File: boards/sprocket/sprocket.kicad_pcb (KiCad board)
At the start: 2 copper layers, 47 x 15 mm, 14 parts, among them U1 STM32G031F8P6

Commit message: I don't know what this branch is
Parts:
- removed the MH at (144.0, 104.0)
- removed the MH at (104.0, 104.0)
- removed the REF** at (125.2, 104.5)
- removed the REF** at (120.0, 103.8)
- removed the REF** at (112.0, 103.8)
- removed the REF** at (129.0, 111.0)
- removed the REF** at (129.0, 112.8)
- removed the REF** at (129.0, 114.5)
- removed the REF** at (132.8, 112.5)
- removed the REF** at (137.5, 112.5)
- removed the REF** at (130.0, 102.8)
- removed the REF** at (109.7, 113.5)
- removed the REF** at (109.7, 111.0)
- removed U1: STM32G031F8P6, footprints:STM32G031F8P6
- added MH: brick-1x2, brick-4_9id-6_0od:brick-1x2, F.Cu at (126.1, 92.0)
- added MH: brick-1x2, brick-4_9id-6_0od:brick-1x2, F.Cu at (166.1, 92.0)
- added REF**: C_0603_1608Metric, Capacitor_SMD:C_0603_1608Metric, F.Cu at (138.5, 101.6)
- added REF**: SW_SPST_PTS810, Button_Switch_SMD:SW_SPST_PTS810, F.Cu at (142.3, 101.0)
- added REF**: SW_SPST_PTS810, Button_Switch_SMD:SW_SPST_PTS810, F.Cu at (142.3, 91.0)
- added REF**: UQFN-28-1EP_4x4mm_P0.4mm_EP2.35x2.35mm, Package_DFN_QFN:UQFN-28-1EP_4x4mm_P0.4mm_EP2.35x2.35mm, F.Cu at (137.3, 96.0)
- added REF**: SOT-23, Package_TO_SOT_SMD:SOT-23, F.Cu at (142.0, 96.0)
- added REF**: JST_SH_BM04B-SRSS-TB_1x04-1MP_P1.00mm_Vertical, Connector_JST:JST_SH_BM04B-SRSS-TB_1x04-1MP_P1.00mm_Vertical, B.Cu at (141.9, 100.8)
- added REF**: JST_SH_BM04B-SRSS-TB_1x04-1MP_P1.00mm_Vertical, Connector_JST:JST_SH_BM04B-SRSS-TB_1x04-1MP_P1.00mm_Vertical, B.Cu at (141.9, 91.2)
- added REF**: JST_SH_SM04B-SRSS-TB_1x04-1MP_P1.00mm_Horizontal, Connector_JST:JST_SH_SM04B-SRSS-TB_1x04-1MP_P1.00mm_Horizontal, B.Cu at (134.1, 100.2)
- added REF**: JST_SH_SM04B-SRSS-TB_1x04-1MP_P1.00mm_Horizontal, Connector_JST:JST_SH_SM04B-SRSS-TB_1x04-1MP_P1.00mm_Horizontal, B.Cu at (134.1, 91.8)
- added REF**: PinHeader_1x06_P2.54mm_Vertical, Connector_PinHeader_2.54mm:PinHeader_1x06_P2.54mm_Vertical, F.Cu at (147.2, 96.0)
- added REF**: PinSocket_2x06_P2.54mm_Horizontal, Connector_PinSocket_2.54mm:PinSocket_2x06_P2.54mm_Horizontal, F.Cu at (147.2, 98.5)
- added REF**: C_0603_1608Metric, Capacitor_SMD:C_0603_1608Metric, F.Cu at (138.5, 90.5)
- added REF**: PinSocket_2x06_P2.54mm_Horizontal, Connector_PinSocket_2.54mm:PinSocket_2x06_P2.54mm_Horizontal, F.Cu at (159.9, 93.5)
- added REF**: R_0603_1608Metric, Resistor_SMD:R_0603_1608Metric, F.Cu at (136.3, 100.8)
- added REF**: R_0603_1608Metric, Resistor_SMD:R_0603_1608Metric, F.Cu at (136.3, 91.2)
- added REF**: C_0603_1608Metric, Capacitor_SMD:C_0603_1608Metric, F.Cu at (144.5, 94.5)
- added REF**: C_0603_1608Metric, Capacitor_SMD:C_0603_1608Metric, F.Cu at (144.5, 97.5)
- added REF**: C_0603_1608Metric, Capacitor_SMD:C_0603_1608Metric, F.Cu at (136.3, 102.3)
- added REF**: C_0603_1608Metric, Capacitor_SMD:C_0603_1608Metric, F.Cu at (136.3, 89.7)
- added REF**: SOT-23, Package_TO_SOT_SMD:SOT-23, F.Cu at (131.9, 96.0)
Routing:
- net (no net): track 0.00 -> 0.25 mm, vias 0 -> 6
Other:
- rule trace_min: 0.2 -> 0.09
- rule via_min_drill: 0.3 -> 0.2
- board text added: "0.0164"
- board text added: "0.0250"
- board text added: "0.0621"
- board text added: "4.2x3.25"
- board text added: "5.1x5.1"
- board text added: "6.0x6.0"
- board text added: "Cheap Round: TS-1187A-C-E-B"
- board text added: "Close, but not EXACTLY footprint as above"
- board text added: "Digital Port"
- board text added: "GND"
- board text added: "GPIO port"
- board text added: "LED"
- board text added: "One Space Horizontal, maybe Vertical"
- board text added: "Oval Switch: K2-1808SN-A4SW-01"
- board text added: "Programming/Debugging Port"
- board text added: "RGB LED"
- board text added: "Round Switch: K2-1102SP-C4SC-04"
- board text added: "SCL"
- board text added: "SDA"
- board text added: "VCC"

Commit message: Work
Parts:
- removed MH (x2): brick-1x2, brick-4_9id-6_0od:brick-1x2
- removed REF** (x6): C_0603_1608Metric, Capacitor_SMD:C_0603_1608Metric
- removed REF** (x2): SW_SPST_PTS810, Button_Switch_SMD:SW_SPST_PTS810
- removed REF**: UQFN-28-1EP_4x4mm_P0.4mm_EP2.35x2.35mm, Package_DFN_QFN:UQFN-28-1EP_4x4mm_P0.4mm_EP2.35x2.35mm
- removed REF** (x2): SOT-23, Package_TO_SOT_SMD:SOT-23
- removed REF** (x2): JST_SH_BM04B-SRSS-TB_1x04-1MP_P1.00mm_Vertical, Connector_JST:JST_SH_BM04B-SRSS-TB_1x04-1MP_P1.00mm_Vertical
- removed REF** (x2): JST_SH_SM04B-SRSS-TB_1x04-1MP_P1.00mm_Horizontal, Connector_JST:JST_SH_SM04B-SRSS-TB_1x04-1MP_P1.00mm_Horizontal
- removed REF**: PinHeader_1x06_P2.54mm_Vertical, Connector_PinHeader_2.54mm:PinHeader_1x06_P2.54mm_Vertical
- removed REF** (x2): PinSocket_2x06_P2.54mm_Horizontal, Connector_PinSocket_2.54mm:PinSocket_2x06_P2.54mm_Horizontal
- removed REF** (x2): R_0603_1608Metric, Resistor_SMD:R_0603_1608Metric
- added C1: 100nF, Capacitor_SMD:C_0402_1005Metric, F.Cu at (117.6, 85.2)
- added C2: 100nF, Capacitor_SMD:C_0402_1005Metric, F.Cu at (117.6, 83.3)
- added C3: 4.7uF, Capacitor_SMD:C_0402_1005Metric, F.Cu at (118.6, 85.2)
- added C4: 1uF, Capacitor_SMD:C_0402_1005Metric, F.Cu at (119.0, 82.6)
- added C5: 2.2uF, Capacitor_SMD:C_0603_1608Metric, F.Cu at (121.5, 85.9)
- added C6: 1uF, Capacitor_SMD:C_0402_1005Metric, F.Cu at (108.6, 87.8)
- added C7: 1uF, Capacitor_SMD:C_0402_1005Metric, F.Cu at (108.6, 77.0)
- added D1: B5819W, Diode_SMD:D_SOD-123, F.Cu at (120.8, 80.4)
- added D2: TC3838RGB, Everything:TC3838RGB, F.Cu at (109.2, 87.0)
- added D3: TC3838RGB, Everything:TC3838RGB, F.Cu at (109.2, 76.2)
- added D4: LED, Diode_SMD:D_0603_1608Metric, F.Cu at (110.5, 84.5)
- added D5: LED, Diode_SMD:D_0603_1608Metric, F.Cu at (109.0, 84.5)
- added D6: LED, Diode_SMD:D_0603_1608Metric, F.Cu at (109.0, 81.2)
- added J1: SPROCKET-CONN, Everything:sprocket-pins, F.Cu at (123.6, 90.6)
- added J4: Conn_01x04_MountingPin, Connector_JST:JST_SH_SM04B-SRSS-TB_1x04-1MP_P1.00mm_Horizontal, B.Cu at (120.7, 87.2)
- added J5: Conn_01x04_MountingPin, Connector_JST:JST_SH_BM04B-SRSS-TB_1x04-1MP_P1.00mm_Vertical, B.Cu at (112.4, 87.9)
- added J6: Conn_01x04_MountingPin, Connector_JST:JST_SH_SM04B-SRSS-TB_1x04-1MP_P1.00mm_Horizontal, B.Cu at (112.4, 78.8)
- added J7: Conn_01x04_MountingPin, Connector_JST:JST_SH_BM04B-SRSS-TB_1x04-1MP_P1.00mm_Vertical, B.Cu at (120.7, 78.1)
- added JP1: SolderJumper_2_Open, Jumper:SolderJumper-2_P1.3mm_Open_TrianglePad1.0x1.5mm, B.Cu at (139.7, 127.0)
- added JP2: SolderJumper_2_Open, Jumper:SolderJumper-2_P1.3mm_Open_TrianglePad1.0x1.5mm, B.Cu at (126.1, 124.7)
- added JP3: SolderJumper_2_Open, Jumper:SolderJumper-2_P1.3mm_Open_TrianglePad1.0x1.5mm, B.Cu at (128.3, 117.6)
- added JP4: SolderJumper_2_Open, Jumper:SolderJumper-2_P1.3mm_Open_TrianglePad1.0x1.5mm, B.Cu at (128.5, 132.0)
- added JP5: SolderJumper_2_Open, Jumper:SolderJumper-2_P1.3mm_Open_TrianglePad1.0x1.5mm, B.Cu at (132.7, 116.3)
- added JP6: SolderJumper_2_Open, Jumper:SolderJumper-2_P1.3mm_Open_TrianglePad1.0x1.5mm, B.Cu at (130.5, 124.7)
- added MH1: Conn_01x02, brick-4_9id-6_0od:brick-1x2, F.Cu at (104.0, 79.0)
- added MH2: Conn_01x02, brick-4_9id-6_0od:brick-1x2, F.Cu at (144.0, 79.0)
- added Q1: NX7002BKR, Package_TO_SOT_SMD:SOT-23, F.Cu at (115.2, 77.5)
- added R1: 10K, Resistor_SMD:R_0402_1005Metric, F.Cu at (116.4, 89.3)
- added R2: 10K, Resistor_SMD:R_0402_1005Metric, F.Cu at (117.5, 76.7)
- added R3: 10K, Resistor_SMD:R_0402_1005Metric, F.Cu at (116.0, 79.8)
- added R4: 1K, Resistor_SMD:R_0402_1005Metric, F.Cu at (117.4, 89.3)
- added R5: 1K, Resistor_SMD:R_0402_1005Metric, F.Cu at (117.5, 78.6)
- added R6: 1K, Resistor_SMD:R_0402_1005Metric, F.Cu at (110.7, 81.5)
- added R7: 1K, Resistor_SMD:R_0402_1005Metric, F.Cu at (110.7, 82.5)
- added R8: 1K, Resistor_SMD:R_0402_1005Metric, F.Cu at (110.7, 80.5)
- added SW1: SW_Push, Everything:K2-1808SN-A4SW-01, F.Cu at (118.2, 87.2)
- added SW2: SW_Push, Everything:K2-1808SN-A4SW-01, F.Cu at (123.8, 78.7)
- added U1: UFQFPN-28, footprints:STM32G031G8U6, F.Cu at (114.4, 84.3)
- added U2: AP2210N-3.3TRG1, Package_TO_SOT_SMD:SOT-23, F.Cu at (121.3, 83.4)
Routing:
- net (no net): track 0.25 -> 0.00 mm, vias 6 -> 0
- added copper zone on B.Cu, net GND
- added copper zone on F.Cu, net GND
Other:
- copper layers 2 -> 4
- rule trace_min: 0.09 -> 0.2
- board text added: "TODO: Move buttons to top, LEDs to bottom"
- board text removed: "0.0164"
- board text removed: "0.0250"
- board text removed: "0.0621"
- board text removed: "4.2x3.25"
- board text removed: "5.1x5.1"
- board text removed: "6.0x6.0"
- board text removed: "Cheap Round: TS-1187A-C-E-B"
- board text removed: "Close, but not EXACTLY footprint as above"
- board text removed: "Digital Port"
- board text removed: "GND"
- board text removed: "GPIO port"
- board text removed: "LED"
- board text removed: "One Space Horizontal, maybe Vertical"
- board text removed: "Oval Switch: K2-1808SN-A4SW-01"
- board text removed: "Programming/Debugging Port"
- board text removed: "RGB LED"
- board text removed: "Round Switch: K2-1102SP-C4SC-04"
- board text removed: "SCL"
- board text removed: "SDA"
- board text removed: "VCC"

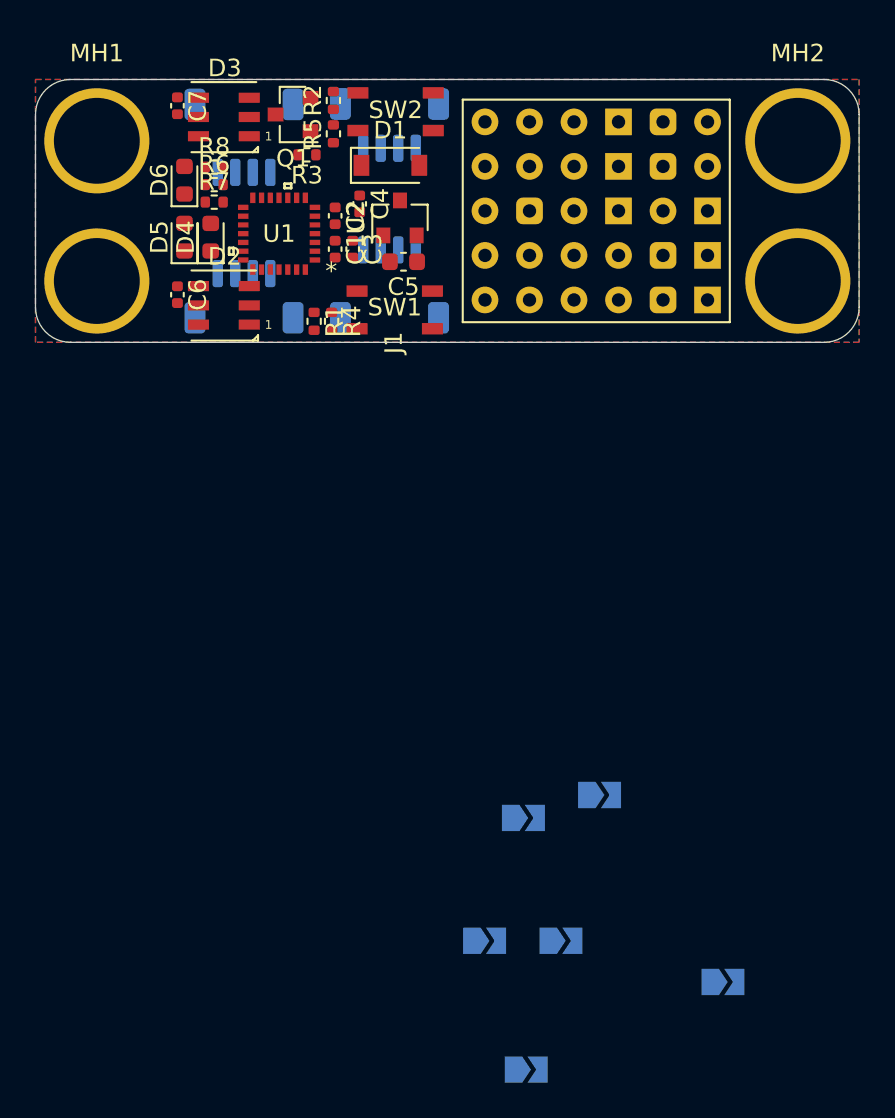
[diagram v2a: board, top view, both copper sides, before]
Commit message: Re-place, pre-route
Trying to keep the 5V low, and the center path clear
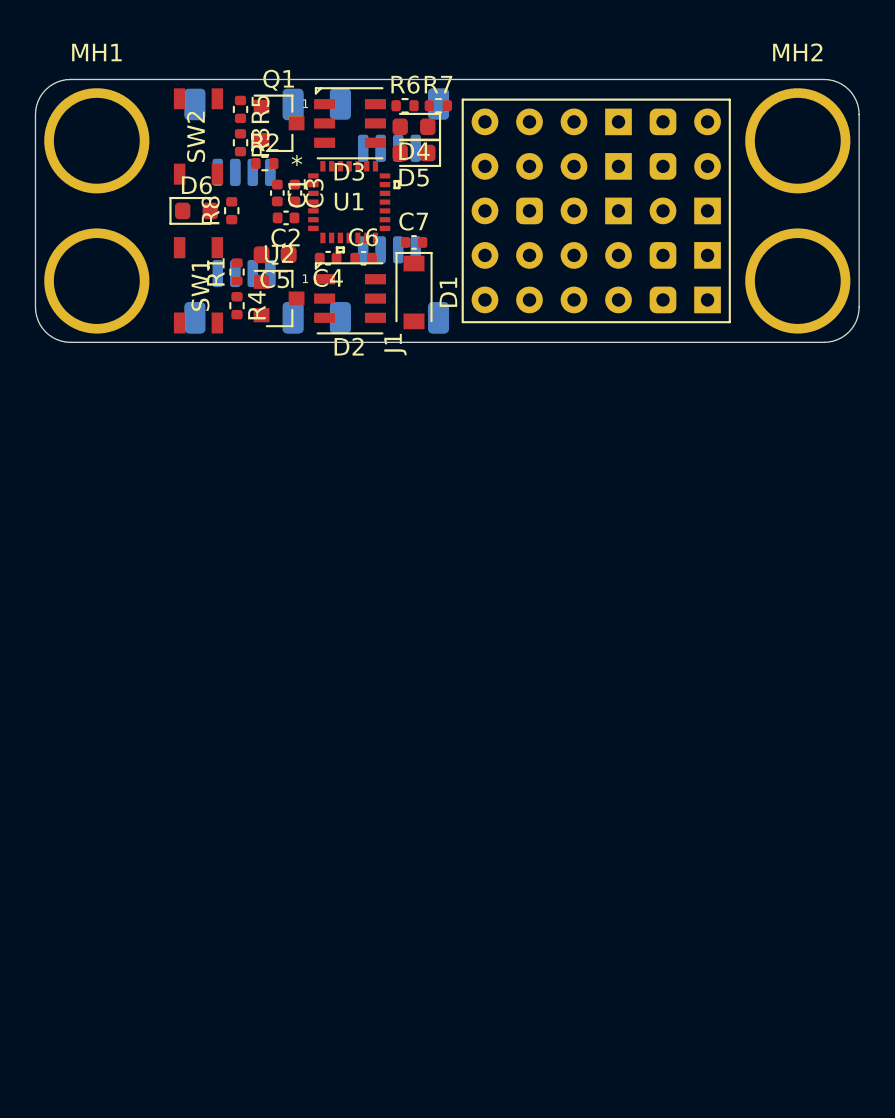
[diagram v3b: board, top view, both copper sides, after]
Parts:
- removed JP1, JP2, JP3, JP4, JP5, JP6: SolderJumper_2_Open, Jumper:SolderJumper-2_P1.3mm_Open_TrianglePad1.0x1.5mm
- U1: value UFQFPN-28 -> STM32G031G8U6
- moved C7 15.6 mm to (122.1, 84.8), turned to 0 degrees
- moved D5 14.0 mm to (122.1, 79.7), turned to 180 degrees
- moved R7 13.9 mm to (123.5, 77.0)
- moved D4 13.2 mm to (122.1, 78.2), turned to 180 degrees
- moved SW2 12.9 mm to (111.2, 76.0), turned to 270 degrees
- moved R6 11.8 mm to (121.6, 77.0)
- moved D3 11.7 mm to (120.5, 79.4), turned to 180 degrees
- moved D2 11.5 mm to (120.5, 89.4), turned to 180 degrees
- moved C6 10.8 mm to (119.2, 85.7), turned to 0 degrees
- moved U2 8.29 mm to (114.4, 88.0), turned to 0 degrees
- moved SW1 7.57 mm to (111.2, 84.5), turned to 270 degrees
- moved D1 7.37 mm to (122.1, 87.7), turned to 270 degrees
- moved C5 7.34 mm to (114.2, 85.5)
- moved R5 5.48 mm to (112.2, 77.2), turned to 270 degrees
- moved R4 5.47 mm to (112.0, 88.4)
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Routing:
- added copper zone on In2.Cu, net +3V3
- added copper zone on In1.Cu, net GND
- removed copper zone on B.Cu, net GND
- removed copper zone on F.Cu, net GND

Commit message: Dead end-ish, going to re-wipe and retry
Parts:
- moved R4 11.2 mm to (112.2, 77.2)
- moved R5 11.2 mm to (112.0, 88.4), turned to 90 degrees
- moved SW1 8.50 mm to (111.2, 76.0)
- moved SW2 8.50 mm to (111.2, 84.5)
- moved R3 2.60 mm to (114.5, 80.3), turned to 180 degrees
- moved R2 1.84 mm to (112.2, 79.1), turned to 270 degrees
- turned R1 to 270 degrees
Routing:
- net GND: track 0.00 -> 53.0 mm, vias 0 -> 9
- net /+5v0-RAW: track 0.00 -> 39.6 mm, vias 0 -> 1
- net +3V3: track 0.00 -> 34.5 mm, vias 0 -> 5
- net /I2C1-SDA: track 0.00 -> 33.9 mm, vias 0 -> 4
- net +5V: track 0.00 -> 31.1 mm
- net /I2C1-SCL: track 0.00 -> 28.4 mm, vias 0 -> 2
- net /~RST: track 0.00 -> 23.6 mm, vias 0 -> 2
- net /GPIO4: track 0.00 -> 17.1 mm, vias 0 -> 2
- net /BUTTON2: track 0.00 -> 16.8 mm, vias 0 -> 2
- net /GPIO3: track 0.00 -> 16.2 mm, vias 0 -> 2
- net /GPIO8: track 0.00 -> 14.4 mm
- net /I2C2-SCL: track 0.00 -> 14.1 mm, vias 0 -> 1
- net /LED1: track 0.00 -> 13.2 mm, vias 0 -> 2
- net /BUTTON1: track 0.00 -> 12.9 mm, vias 0 -> 2
- net /SMARTLED-3V3: track 0.00 -> 12.5 mm, vias 0 -> 2
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- added copper zone on B.Cu, net GND

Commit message: Gunna bail.
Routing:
- net +5V: track 31.1 -> 67.0 mm, vias 0 -> 6
- net /UART-TX: track 0.00 -> 32.6 mm, vias 0 -> 2
- net /UART-RX: track 0.00 -> 28.0 mm, vias 0 -> 2
- net +3V3: track 34.5 -> 61.2 mm, vias 5 -> 6
- net /+5v0-RAW: track 39.6 -> 55.3 mm, vias 1 -> 2
- net /SPI-CIPO: track 0.00 -> 13.4 mm, vias 0 -> 2
- net /GPIO1: track 0.00 -> 13.3 mm, vias 0 -> 1
- net /SPI-SCK: track 0.00 -> 13.1 mm, vias 0 -> 1
- net /GPIO2: track 0.00 -> 12.5 mm, vias 0 -> 1
- net GND: track 53.0 -> 64.7 mm, vias 9 -> 5
- net Net-(D5-Pad2): track 0.00 -> 11.6 mm, vias 0 -> 3
- net /SPI-COPI: track 0.00 -> 9.71 mm, vias 0 -> 1
- net /~SPI-CS: track 0.00 -> 7.83 mm
- net /QWIIC2-SCL: track 6.62 -> 9.66 mm
- net /I2C1-SDA: track 33.9 -> 31.3 mm, vias 4 -> 3
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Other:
- board text removed: "TODO: Move buttons to top, LEDs to bottom"

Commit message: About to give up again
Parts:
- removed R1: 10K, Resistor_SMD:R_0402_1005Metric
- added JP3: SolderJumper_2_Open, Jumper:SolderJumper-2_P1.3mm_Open_RoundedPad1.0x1.5mm, F.Cu at (106.2, 83.0)
- added JP4: SolderJumper_2_Open, Jumper:SolderJumper-2_P1.3mm_Open_RoundedPad1.0x1.5mm, F.Cu at (101.8, 83.0)
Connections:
- J6 pad 3: /QWIIC2-SDA -> /I2C2-SDA
- J6 pad 4: /QWIIC2-SCL -> /I2C2-SCL
- J7 pad 3: /QWIIC2-SDA -> /I2C2-SDA
- J7 pad 4: /QWIIC2-SCL -> /I2C2-SCL
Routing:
- net /I2C2-SDA: track 11.4 -> 31.6 mm, vias 1 -> 5
- net /I2C2-SCL: track 16.0 -> 33.9 mm, vias 1 -> 3
- net /+5v0-RAW: track 55.3 -> 71.3 mm
- net +3V3: track 61.2 -> 46.5 mm, vias 6 -> 3
- net GND: track 64.7 -> 50.9 mm, vias 5 -> 11
- net +5V: track 67.0 -> 55.2 mm, vias 6 -> 4
- net /QWIIC2-SDA: track 11.5 -> 0.00 mm
- net /QWIIC2-SCL: track 9.66 -> 0.00 mm
- net /I2C1-SCL: track 27.2 -> 32.7 mm, vias 2 -> 3
- net /BUTTON2: track 18.1 -> 13.6 mm
- net Net-(D5-Pad2): track 11.6 -> 7.36 mm, vias 3 -> 0
- net /I2C1-SDA: track 31.3 -> 27.9 mm
- net /SPI-SCK: track 13.1 -> 10.5 mm
- net /GPIO8: track 16.9 -> 14.4 mm, vias 1 -> 0
- net /SPI-CIPO: track 13.4 -> 11.6 mm, vias 2 -> 1
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
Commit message: Everything but the LEDs
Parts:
- moved R7 11.8 mm to (114.7, 84.8), turned to 90 degrees
- moved R6 11.6 mm to (112.9, 84.8), turned to 180 degrees
- moved D3 9.99 mm to (121.0, 89.4)
- moved Q1 9.22 mm to (121.8, 83.5), turned to 270 degrees
- moved D4 8.46 mm to (123.9, 69.9)
- moved R2 8.21 mm to (119.5, 82.9)
- moved R5 6.48 mm to (113.9, 82.2), turned to 0 degrees
- moved D5 6.24 mm to (117.1, 83.4), turned to 270 degrees
- moved C4 6.15 mm to (111.1, 85.8), turned to 0 degrees
- moved R3 6.11 mm to (119.0, 84.4), turned to 0 degrees
- moved C7 5.88 mm to (116.3, 85.4)
- moved R4 5.41 mm to (110.1, 82.2), turned to 180 degrees
- moved C5 4.87 mm to (109.3, 84.8), turned to 90 degrees
- moved C1 4.37 mm to (116.3, 78.1)
- moved C2 4.36 mm to (116.8, 79.5)
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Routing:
- net /+5v0-RAW: track 71.3 -> 57.6 mm, vias 2 -> 1
- net +5V: track 55.2 -> 68.2 mm, vias 4 -> 1
- net /LED1: track 12.5 -> 0.00 mm, vias 2 -> 0
- net /UART-TX: track 33.1 -> 21.3 mm
- net Net-(D2-Pad3): track 0.00 -> 10.4 mm, vias 0 -> 2
- net /I2C1-SDA: track 27.9 -> 38.2 mm, vias 3 -> 4
- net /LED2: track 8.44 -> 0.00 mm, vias 2 -> 0
- net /SMARTLED-3V3: track 11.7 -> 4.11 mm, vias 2 -> 0
- net /~RST: track 25.3 -> 32.7 mm, vias 1 -> 2
- net /UART-RX: track 28.5 -> 21.7 mm
- net GND: track 50.9 -> 56.0 mm
- net /SMARTLED-5V0: track 5.38 -> 9.94 mm, vias 0 -> 2
- net Net-(D5-Pad2): track 7.36 -> 2.84 mm
- net /I2C2-SCL: track 33.9 -> 37.4 mm
- net /I2C1-SCL: track 32.7 -> 36.1 mm, vias 3 -> 4
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
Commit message: seems done?
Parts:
- moved D4 15.7 mm to (115.9, 83.4), turned to 270 degrees
- moved D5 0.25 mm to (117.3, 83.4)
- moved R7 0.22 mm to (114.6, 85.0)
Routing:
- net /LED1: track 0.00 -> 15.4 mm, vias 0 -> 2
- net /LED2: track 0.00 -> 9.59 mm, vias 0 -> 2
- net Net-(D4-Pad2): track 0.00 -> 4.44 mm, vias 0 -> 2
- net +3V3: track 49.8 -> 54.0 mm
- net /I2C2-SCL: track 37.4 -> 34.5 mm, vias 3 -> 4
- net Net-(D5-Pad2): track 2.84 -> 4.39 mm, vias 0 -> 2
- net GND: track 56.0 -> 57.3 mm
- net /~RST: track 32.7 -> 31.5 mm
- net /GPIO1: track 11.7 -> 12.5 mm
- net /+5v0-RAW: track 57.6 -> 57.0 mm
- net /UART-TX: track 21.3 -> 21.9 mm
- net /I2C1-SDA: track 38.2 -> 38.8 mm
